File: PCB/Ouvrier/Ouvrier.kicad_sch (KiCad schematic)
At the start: 7 parts, among them Q1 2N2220, U1 XIAO-ESP32-S3-Plus-SMD, U2 BMP581, U3 UWB

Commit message: MaJ KiCad ouvrier bibliotheque
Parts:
- removed LS1: CMT-8504-100-SMT-TR, Library:CMT8504100SMTTR, symbol CMT-8504-100-SMT-TR:CMT-8504-100-SMT-TR
- added J1: Conn_01x02, Bibliotheque_Projet:CONN-TH_2P-P5.00_L7.6-W10.0, symbol Connector_Generic:Conn_01x02
- added LS2: CMT-8504-100-SMT-TR, Bibliotheque_Projet:Buzzer CMS, symbol Bibliotheque_Projet:CMT-8504-100-SMT-TR
- U3: footprint Library:UWB -> Bibliotheque_Projet:maUWB chipset; symbol UWB:UWB -> Bibliotheque_Projet:maUWB AT chipset
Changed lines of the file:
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@@
+	)
+	(junction
+		(at 251.46 35.56)
+		(diameter 0)
+		(color 0 0 0 0)
 	)
 	(junction
@@
 		(color 0 0 0 0)
 	)
-	(junction
-		(at 251.46 35.56)
-		(diameter 0)
-		(color 0 0 0 0)
-	)
 	(wire
 		(pts
@@
 			(width 0)
 			(type default)
-		)
-	)
-	(symbol
-		(lib_id "CMT-8504-100-SMT-TR:CMT-8504-100-SMT-TR")
-		(at 246.38 121.92 0)
-		(unit 1)
-		(body_style 1)
-		(exclude_from_sim no)
-		(in_bom yes)
-		(on_board yes)
-		(in_pos_files yes)
-		(dnp no)
-		(fields_autoplaced yes)
-		(property "Reference" "LS1"
-			(at 262.89 114.3 0)
-			(show_name no)
-			(do_not_autoplace no)
-			(effects
-				(font
-					(size 1.27 1.27)
-				)
-			)
-		)
-		(property "Value" "CMT-8504-100-SMT-TR"
-			(at 262.89 116.84 0)
-			(show_name no)
-			(do_not_autoplace no)
-			(effects
-				(font
-					(size 1.27 1.27)
-				)
-			)
-		)
-		(property "Footprint" "Library:CMT8504100SMTTR"
-			(at 275.59 216.84 0)
-			(hide yes)
-			(show_name no)
-			(do_not_autoplace no)
-			(effects
-				(font
-					(size 1.27 1.27)
-				)
-				(justify left top)
-			)
-		)
-		(property "Datasheet" "https://www.sameskydevices.com/product/resource/cmt-8504-100-smt-tr.pdf"
-			(at 275.59 316.84 0)
-			(hide yes)
-			(show_name no)
-			(do_not_autoplace no)
-			(effects
-				(font
-					(size 1.27 1.27)
-				)
-				(justify left top)
-			)
-		)
-		(property "Description" "8.5 mm, 5 Vo-p, 100 dB, Surface Mount (SMT), Magnetic Audio Transducer Buzzer"
-			(at 246.38 121.92 0)
-			(hide yes)
-			(show_name no)
-			(do_not_autoplace no)
-			(effects
-				(font
-					(size 1.27 1.27)
-				)
-			)
-		)
-		(property "Height" "4.5"
-			(at 275.59 516.84 0)
-			(hide yes)
-			(show_name no)
-			(do_not_autoplace no)
-			(effects
-				(font
-					(size 1.27 1.27)
-				)
-				(justify left top)
-			)
-		)
-		(property "Manufacturer_Name" "Same Sky"
-			(at 275.59 616.84 0)
-			(hide yes)
-			(show_name no)
-			(do_not_autoplace no)
-			(effects
-				(font
-					(size 1.27 1.27)
-				)
-				(justify left top)
-			)
-		)
-		(property "Manufacturer_Part_Number" "CMT-8504-100-SMT-TR"
-			(at 275.59 716.84 0)
-			(hide yes)
-			(show_name no)
-			(do_not_autoplace no)
-			(effects
-				(font
-					(size 1.27 1.27)
-				)
-				(justify left top)
-			)
-		)
-		(property "Mouser Part Number" "490-CMT-8504100SMTTR"
-			(at 275.59 816.84 0)
-			(hide yes)
-			(show_name no)
-			(do_not_autoplace no)
-			(effects
-				(font
-					(size 1.27 1.27)
-				)
-				(justify left top)
-			)
-		)
-		(property "Mouser Price/Stock" "https://www.mouser.co.uk/ProductDetail/Same-Sky/CMT-8504-100-SMT-TR?qs=P1JMDcb91o7N%2FrNVZpuJrw%3D%3D"
-			(at 275.59 916.84 0)
-			(hide yes)
-			(show_name no)
-			(do_not_autoplace no)
-			(effects
-				(font
-					(size 1.27 1.27)
-				)
-				(justify left top)
-			)
-		)
-		(property "Arrow Part Number" "CMT-8504-100-SMT-TR"
-			(at 275.59 1016.84 0)
-			(hide yes)
-			(show_name no)
-			(do_not_autoplace no)
-			(effects
-				(font
-					(size 1.27 1.27)
-				)
-				(justify left top)
-			)
-		)
-		(property "Arrow Price/Stock" "https://www.arrow.com/en/products/cmt-8504-100-smt-tr/cui-devices.html?utm_currency=USD&region=nac"
-			(at 275.59 1116.84 0)
-			(hide yes)
-			(show_name no)
-			(do_not_autoplace no)
-			(effects
-				(font
-					(size 1.27 1.27)
-				)
-				(justify left top)
-			)
-		)
-		(pin "1"
-		)
-		(pin "3"
-		)
-		(pin "4"
-		)
-		(pin "2"
-		)
-		(instances
-			(project "Ouvrier"
-				(path "/84605c1a-5009-408b-9a0f-13132cab7487"
-					(reference "LS1")
-					(unit 1)
-				)
-			)
 		)
 	)
@@
 	)
 	(symbol
+		(lib_id "Bibliotheque_Projet:CMT-8504-100-SMT-TR")
+		(at 240.03 113.03 0)
+		(unit 1)
+		(body_style 1)
+		(exclude_from_sim no)
+		(in_bom yes)
+		(on_board yes)
+		(in_pos_files yes)
+		(dnp no)
+		(fields_autoplaced yes)
+		(property "Reference" "LS2"
+			(at 256.54 105.41 0)
+			(show_name no)
+			(do_not_autoplace no)
+			(effects
+				(font
+					(size 1.27 1.27)
+				)
+			)
+		)
+		(property "Value" "CMT-8504-100-SMT-TR"
+			(at 256.54 107.95 0)
+			(show_name no)
+			(do_not_autoplace no)
+			(effects
+				(font
+					(size 1.27 1.27)
+				)
+			)
+		)
+		(property "Footprint" "Bibliotheque_Projet:Buzzer CMS"
+			(at 269.24 207.95 0)
+			(hide yes)
+			(show_name no)
+			(do_not_autoplace no)
+			(effects
+				(font
+					(size 1.27 1.27)
+				)
+				(justify left top)
+			)
+		)
+		(property "Datasheet" "https://www.sameskydevices.com/product/resource/cmt-8504-100-smt-tr.pdf"
+			(at 269.24 307.95 0)
+			(hide yes)
+			(show_name no)
+			(do_not_autoplace no)
+			(effects
+				(font
+					(size 1.27 1.27)
+				)
+				(justify left top)
+			)
+		)
+		(property "Description" "8.5 mm, 5 Vo-p, 100 dB, Surface Mount (SMT), Magnetic Audio Transducer Buzzer"
+			(at 240.03 113.03 0)
+			(hide yes)
+			(show_name no)
+			(do_not_autoplace no)
+			(effects
+				(font
+					(size 1.27 1.27)
+				)
+			)
+		)
+		(property "Height" "4.5"
+			(at 269.24 507.95 0)
+			(hide yes)
+			(show_name no)
+			(do_not_autoplace no)
+			(effects
+				(font
+					(size 1.27 1.27)
+				)
+				(justify left top)
+			)
+		)
+		(property "Manufacturer_Name" "Same Sky"
+			(at 269.24 607.95 0)
+			(hide yes)
+			(show_name no)
+			(do_not_autoplace no)
+			(effects
+				(font
+					(size 1.27 1.27)
+				)
+				(justify left top)
+			)
+		)
+		(property "Manufacturer_Part_Number" "CMT-8504-100-SMT-TR"
+			(at 269.24 707.95 0)
+			(hide yes)
+			(show_name no)
+			(do_not_autoplace no)
+			(effects
+				(font
+					(size 1.27 1.27)
+				)
+				(justify left top)
+			)
+		)
+		(property "Mouser Part Number" "490-CMT-8504100SMTTR"
+			(at 269.24 807.95 0)
+			(hide yes)
+			(show_name no)
+			(do_not_autoplace no)
+			(effects
+				(font
+					(size 1.27 1.27)
+				)
+				(justify left top)
+			)
+		)
+		(property "Mouser Price/Stock" "https://www.mouser.co.uk/ProductDetail/Same-Sky/CMT-8504-100-SMT-TR?qs=P1JMDcb91o7N%2FrNVZpuJrw%3D%3D"
+			(at 269.24 907.95 0)
+			(hide yes)
+			(show_name no)
+			(do_not_autoplace no)
+			(effects
+				(font
+					(size 1.27 1.27)
+				)
+				(justify left top)
+			)
+		)
+		(property "Arrow Part Number" "CMT-8504-100-SMT-TR"
+			(at 269.24 1007.95 0)
+			(hide yes)
+			(show_name no)
+			(do_not_autoplace no)
+			(effects
+				(font
+					(size 1.27 1.27)
+				)
+				(justify left top)
+			)
+		)
+		(property "Arrow Price/Stock" "https://www.arrow.com/en/products/cmt-8504-100-smt-tr/cui-devices.html?utm_currency=USD&region=nac"
+			(at 269.24 1107.95 0)
+			(hide yes)
+			(show_name no)
+			(do_not_autoplace no)
+			(effects
+				(font
+					(size 1.27 1.27)
+				)
+				(justify left top)
+			)
+		)
+		(pin "2"
+		)
+		(pin "3"
+		)
+		(pin "4"
+		)
+		(pin "1"
+		)
+		(instances
+			(project "Ouvrier"
+				(path "/84605c1a-5009-408b-9a0f-13132cab7487"
+					(reference "LS2")
+					(unit 1)
+				)
+			)
+		)
+	)
+	(symbol
 		(lib_id "power:GNDREF")
 		(at 72.39 118.11 0)
@@
 	)
 	(symbol
-		(lib_id "UWB:UWB")
+		(lib_id "Connector_Generic:Conn_01x02")
+		(at 49.53 39.37 0)
+		(unit 1)
+		(body_style 1)
+		(exclude_from_sim no)
+		(in_bom yes)
+		(on_board yes)
+		(in_pos_files yes)
+		(dnp no)
+		(fields_autoplaced yes)
+		(property "Reference" "J1"
+			(at 52.07 39.3699 0)
+			(show_name no)
+			(do_not_autoplace no)
+			(effects
+				(font
+					(size 1.27 1.27)
+				)
+				(justify left)
+			)
+		)
+		(property "Value" "Conn_01x02"
+			(at 52.07 41.9099 0)
+			(show_name no)
+			(do_not_autoplace no)
+			(effects
+				(font
+					(size 1.27 1.27)
+				)
+				(justify left)
+			)
+		)
+		(property "Footprint" "Bibliotheque_Projet:CONN-TH_2P-P5.00_L7.6-W10.0"
+			(at 49.53 39.37 0)
+			(hide yes)
+			(show_name no)
+			(do_not_autoplace no)
+			(effects
+				(font
+					(size 1.27 1.27)
+				)
+			)
+		)
+		(property "Datasheet" ""
+			(at 49.53 39.37 0)
+			(hide yes)
+			(show_name no)
+			(do_not_autoplace no)
+			(effects
+				(font
+					(size 1.27 1.27)
+				)
+			)
+		)
+		(property "Description" "Generic connector, single row, 01x02, script generated (kicad-library-utils/schlib/autogen/connector/)"
+			(at 49.53 39.37 0)
+			(hide yes)
+			(show_name no)
+			(do_not_autoplace no)
+			(effects
+				(font
+					(size 1.27 1.27)
+				)
+			)
+		)
+		(pin "2"
+		)
+		(pin "1"
+		)
+		(instances
+			(project "Ouvrier"
+				(path "/84605c1a-5009-408b-9a0f-13132cab7487"
+					(reference "J1")
+					(unit 1)
+				)
+			)
+		)
+	)
+	(symbol
+		(lib_id "Bibliotheque_Projet:maUWB AT chipset")
 		(at 238.76 44.45 0)
 		(unit 1)
@@
 			)
 		)
-		(property "Footprint" "Library:UWB"
+		(property "Footprint" "Bibliotheque_Projet:maUWB chipset"
 			(at 245.745 44.45 90)
 			(hide yes)

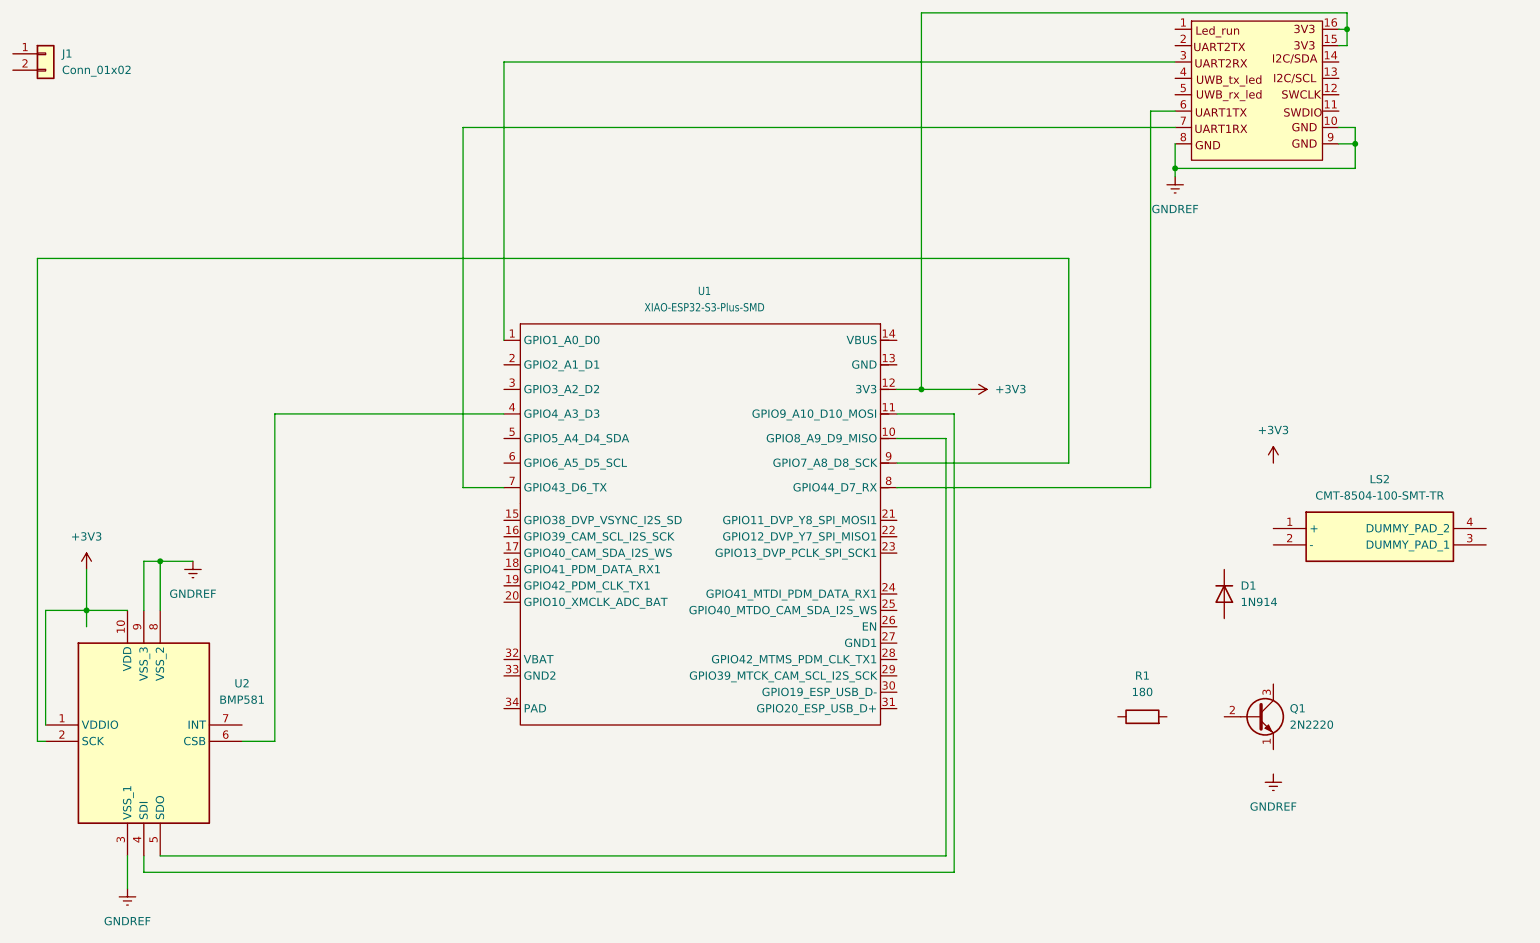
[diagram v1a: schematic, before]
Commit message: MaJ KiCad Ouvrier Xiao DIP et bibliotheque
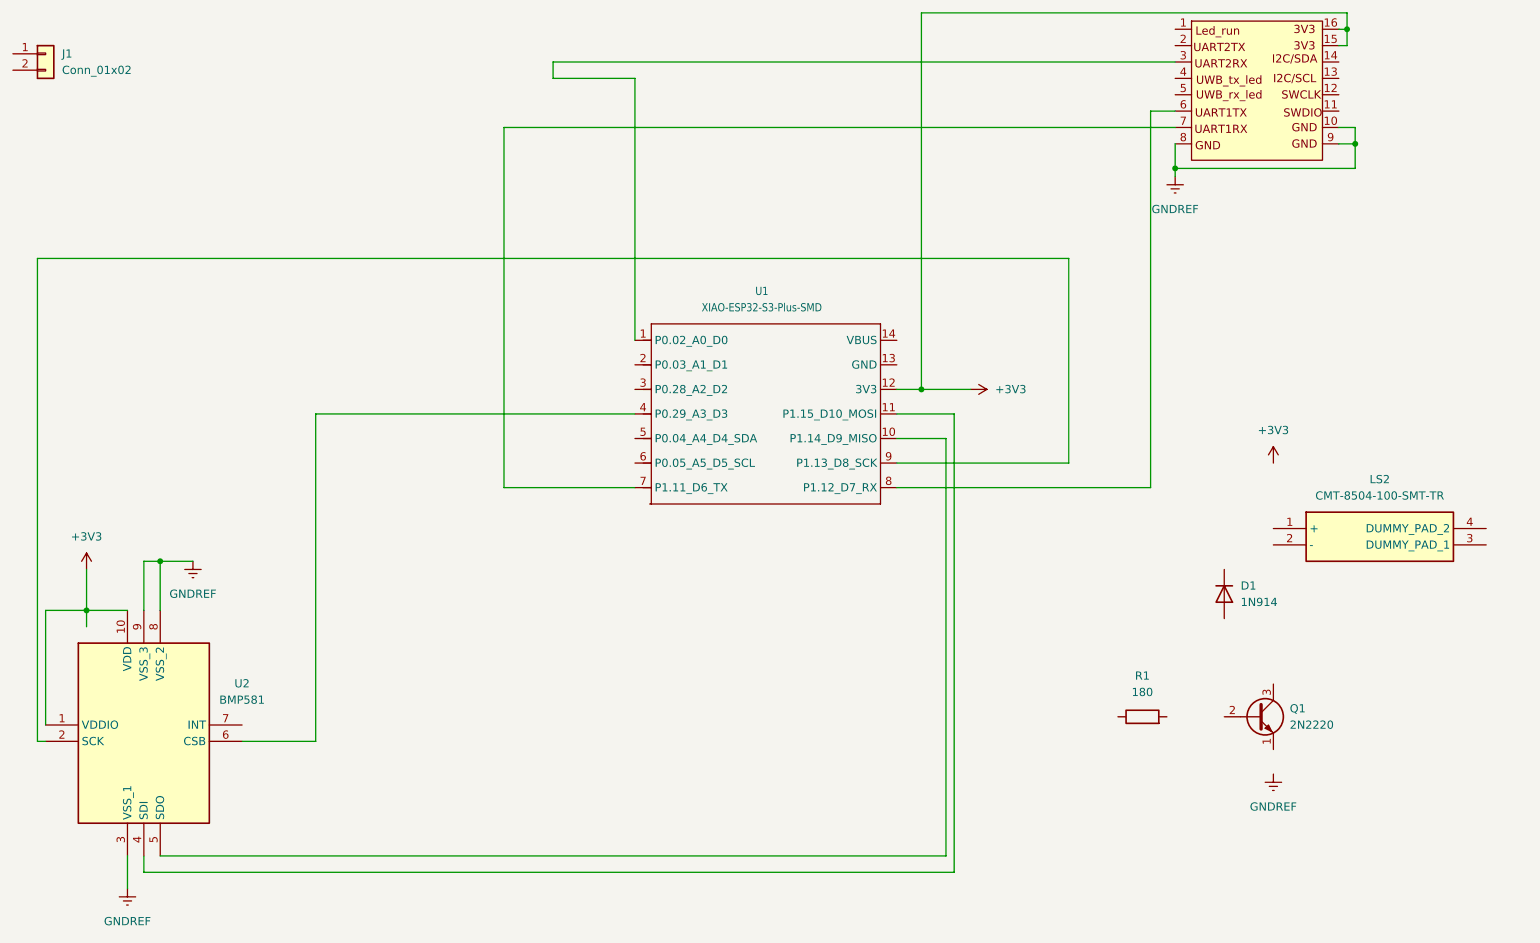
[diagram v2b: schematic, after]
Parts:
- U1: footprint Seeed_Studio_XIAO_Series:XIAO-ESP32-S3-Plus-SMD -> Bibliotheque_Projet:XIAO nRF52840 sense plus; symbol Seeed_Studio_XIAO_Series:XIAO-ESP32-S3 Plus-SMD -> Bibliotheque_Projet:XIAO-nRF52840-DIP
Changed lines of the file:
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@@
 	(wire
 		(pts
-			(xy 114.3 106.68) (xy 114.3 50.8)
+			(xy 120.65 106.68) (xy 120.65 50.8)
 		)
 		(stroke
@@
 	(wire
 		(pts
-			(xy 120.65 95.25) (xy 85.09 95.25)
+			(xy 140.97 95.25) (xy 91.44 95.25)
 		)
 		(stroke
@@
 	(wire
 		(pts
-			(xy 120.65 106.68) (xy 114.3 106.68)
-		)
-		(stroke
-			(width 0)
-			(type default)
-		)
-	)
-	(wire
-		(pts
-			(xy 114.3 50.8) (xy 224.79 50.8)
+			(xy 140.97 106.68) (xy 120.65 106.68)
+		)
+		(stroke
+			(width 0)
+			(type default)
+		)
+	)
+	(wire
+		(pts
+			(xy 120.65 50.8) (xy 224.79 50.8)
 		)
 		(stroke
@@
 	(wire
 		(pts
-			(xy 120.65 40.64) (xy 224.79 40.64)
-		)
-		(stroke
-			(width 0)
-			(type default)
-		)
-	)
-	(wire
-		(pts
-			(xy 85.09 95.25) (xy 85.09 146.05)
+			(xy 140.97 43.18) (xy 128.27 43.18)
+		)
+		(stroke
+			(width 0)
+			(type default)
+		)
+	)
+	(wire
+		(pts
+			(xy 91.44 95.25) (xy 91.44 146.05)
 		)
 		(stroke
@@
 	(wire
 		(pts
+			(xy 128.27 43.18) (xy 128.27 40.64)
+		)
+		(stroke
+			(width 0)
+			(type default)
+		)
+	)
+	(wire
+		(pts
 			(xy 224.79 57.15) (xy 252.73 57.15)
 		)
@@
 	(wire
 		(pts
+			(xy 128.27 40.64) (xy 224.79 40.64)
+		)
+		(stroke
+			(width 0)
+			(type default)
+		)
+	)
+	(wire
+		(pts
 			(xy 48.26 71.12) (xy 48.26 146.05)
 		)
@@
 	(wire
 		(pts
-			(xy 120.65 83.82) (xy 120.65 40.64)
+			(xy 140.97 83.82) (xy 140.97 43.18)
 		)
 		(stroke
@@
 	(wire
 		(pts
-			(xy 85.09 146.05) (xy 80.01 146.05)
+			(xy 91.44 146.05) (xy 80.01 146.05)
 		)
 		(stroke
@@
 	)
 	(symbol
-		(lib_id "Seeed_Studio_XIAO_Series:XIAO-ESP32-S3 Plus-SMD")
-		(at 144.78 95.25 0)
+		(lib_id "Bibliotheque_Projet:XIAO-nRF52840-DIP")
+		(at 147.32 80.01 0)
 		(unit 1)
 		(body_style 1)
@@
 		(fields_autoplaced yes)
 		(property "Reference" "U1"
-			(at 151.765 76.2 0)
+			(at 160.655 76.2 0)
 			(show_name no)
 			(do_not_autoplace no)
@@
 		)
 		(property "Value" "XIAO-ESP32-S3-Plus-SMD"
-			(at 151.765 78.74 0)
+			(at 160.655 78.74 0)
 			(show_name no)
 			(do_not_autoplace no)
@@
 			)
 		)
-		(property "Footprint" "Seeed_Studio_XIAO_Series:XIAO-ESP32-S3-Plus-SMD"
-			(at 154.432 88.646 0)
+		(property "Footprint" "Bibliotheque_Projet:XIAO nRF52840 sense plus"
+			(at 160.02 110.744 0)
+			(hide yes)
+			(show_name no)
+			(do_not_autoplace no)
+			(effects
+				(font
+					(size 1.27 1.27)
+				)
+			)
+		)
+		(property "Datasheet" ""
+			(at 143.51 77.47 0)
+			(hide yes)
+			(show_name no)
+			(do_not_autoplace no)
+			(effects
+				(font
+					(size 1.27 1.27)
+				)
+			)
+		)
+		(property "Description" "XIAO-HALF-HOLE-33P"
+			(at 143.51 77.47 0)
+			(hide yes)
+			(show_name no)
+			(do_not_autoplace no)
+			(effects
+				(font
+					(size 1.27 1.27)
+				)
+			)
+		)
+		(property "Manufacturer" ""
+			(at 147.32 80.01 0)
 			(hide yes)
 			(show_name no)
@@
 			)
 		)
-		(property "Datasheet" ""
-			(at 144.78 95.25 0)
+		(property "MPN" ""
+			(at 147.32 80.01 0)
 			(hide yes)
 			(show_name no)
@@
 			)
 		)
-		(property "Description" "XIAO-HALF-HOLE-33P"
-			(at 152.146 92.964 0)
+		(property "SKU" "XIAO-HALF-HOLE-33P"
+			(at 153.924 89.662 0)
 			(hide yes)
 			(show_name no)
@@
 			)
 		)
-		(property "Manufacturer" ""
-			(at 144.78 95.25 0)
+		(property "Part Type" ""
+			(at 147.32 80.01 0)
 			(hide yes)
 			(show_name no)
@@
 			)
 		)
-		(property "MPN" ""
-			(at 144.78 95.25 0)
-			(hide yes)
+		(property "Rating" ""
+			(at 147.32 80.01 0)
 			(show_name no)
 			(do_not_autoplace no)
@@
 			)
 		)
-		(property "SKU" "XIAO-HALF-HOLE-33P"
-			(at 151.384 104.902 0)
+		(property "Status" ""
+			(at 147.32 80.01 0)
 			(hide yes)
 			(show_name no)
@@
 			)
 		)
-		(property "Part Type" ""
-			(at 144.78 95.25 0)
+		(property "Temperature" ""
+			(at 147.32 80.01 0)
 			(hide yes)
 			(show_name no)
@@
 			)
 		)
-		(property "Rating" ""
-			(at 144.78 95.25 0)
+		(property "Priority" ""
+			(at 147.32 80.01 0)
+			(hide yes)
 			(show_name no)
 			(do_not_autoplace no)
@@
 			)
 		)
-		(property "Status" ""
-			(at 144.78 95.25 0)
-			(hide yes)
-			(show_name no)
-			(do_not_autoplace no)
-			(effects
-				(font
-					(size 1 1)
-				)
-			)
-		)
-		(property "Temperature" ""
-			(at 144.78 95.25 0)
-			(hide yes)
-			(show_name no)
-			(do_not_autoplace no)
-			(effects
-				(font
-					(size 1 1)
-				)
-			)
-		)
-		(property "Priority" ""
-			(at 144.78 95.25 0)
-			(hide yes)
-			(show_name no)
-			(do_not_autoplace no)
-			(effects
-				(font
-					(size 1 1)
-				)
-			)
-		)
 		(pin "1"
 		)
-		(pin "16"
-		)
 		(pin "7"
 		)
@@
 		(pin "4"
 		)
-		(pin "19"
-		)
-		(pin "26"
-		)
 		(pin "14"
 		)
-		(pin "29"
-		)
-		(pin "31"
-		)
-		(pin "34"
-		)
 		(pin "2"
 		)
-		(pin "18"
-		)
 		(pin "12"
 		)
 		(pin "13"
 		)
-		(pin "24"
-		)
-		(pin "32"
-		)
-		(pin "22"
-		)
 		(pin "3"
 		)
@@
 		(pin "8"
 		)
-		(pin "15"
-		)
-		(pin "20"
-		)
-		(pin "17"
-		)
-		(pin "23"
-		)
-		(pin "21"
-		)
-		(pin "25"
-		)
-		(pin "27"
-		)
-		(pin "28"
-		)
-		(pin "30"
-		)
-		(pin "33"
-		)
 		(instances
